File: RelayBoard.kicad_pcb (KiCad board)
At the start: 4 copper layers, 210.4 x 94.7 mm, 103 parts, among them J1 CONN_03-SCREW-5MM, J10 24VAC Input, J11 CONN_03-SCREW-5MM, J12 CONN_03-SCREW-5MM, J13 CONN_03-SCREW-5MM, J14 CONN_03-SCREW-5MM, J15 CONN_03-SCREW-5MM, J16 CONN_03-SCREW-5MM, J17 CONN_03-SCREW-5MM, J18 CONN_03-SCREW-5MM, J19 Raspberry_Pi_2_3, J2 CONN_03-SCREW-5MM, J22 Conn_01x04, J24 Conn_01x06, J3 CONN_03-SCREW-5MM, J4 CONN_03-SCREW-5MM, J5 CONN_03-SCREW-5MM, J6 CONN_03-SCREW-5MM, J7 CONN_03-SCREW-5MM, J8 CONN_03-SCREW-5MM, J9 DC Input, Q1 ULN2803ADWR, Q2 ULN2803ADWR, U1 TLP148G, U11 TLP148G, U12 TLP148G, U13 TLP148G, U14 TLP148G, U15 TLP148G, U16 TLP148G, U17 TLP148G, U18 TLP148G, U2 TLP148G, U3 TLP148G, U4 TLP148G, U5 TLP148G, U6 TLP148G, U7 TLP148G, U8 TLP148G

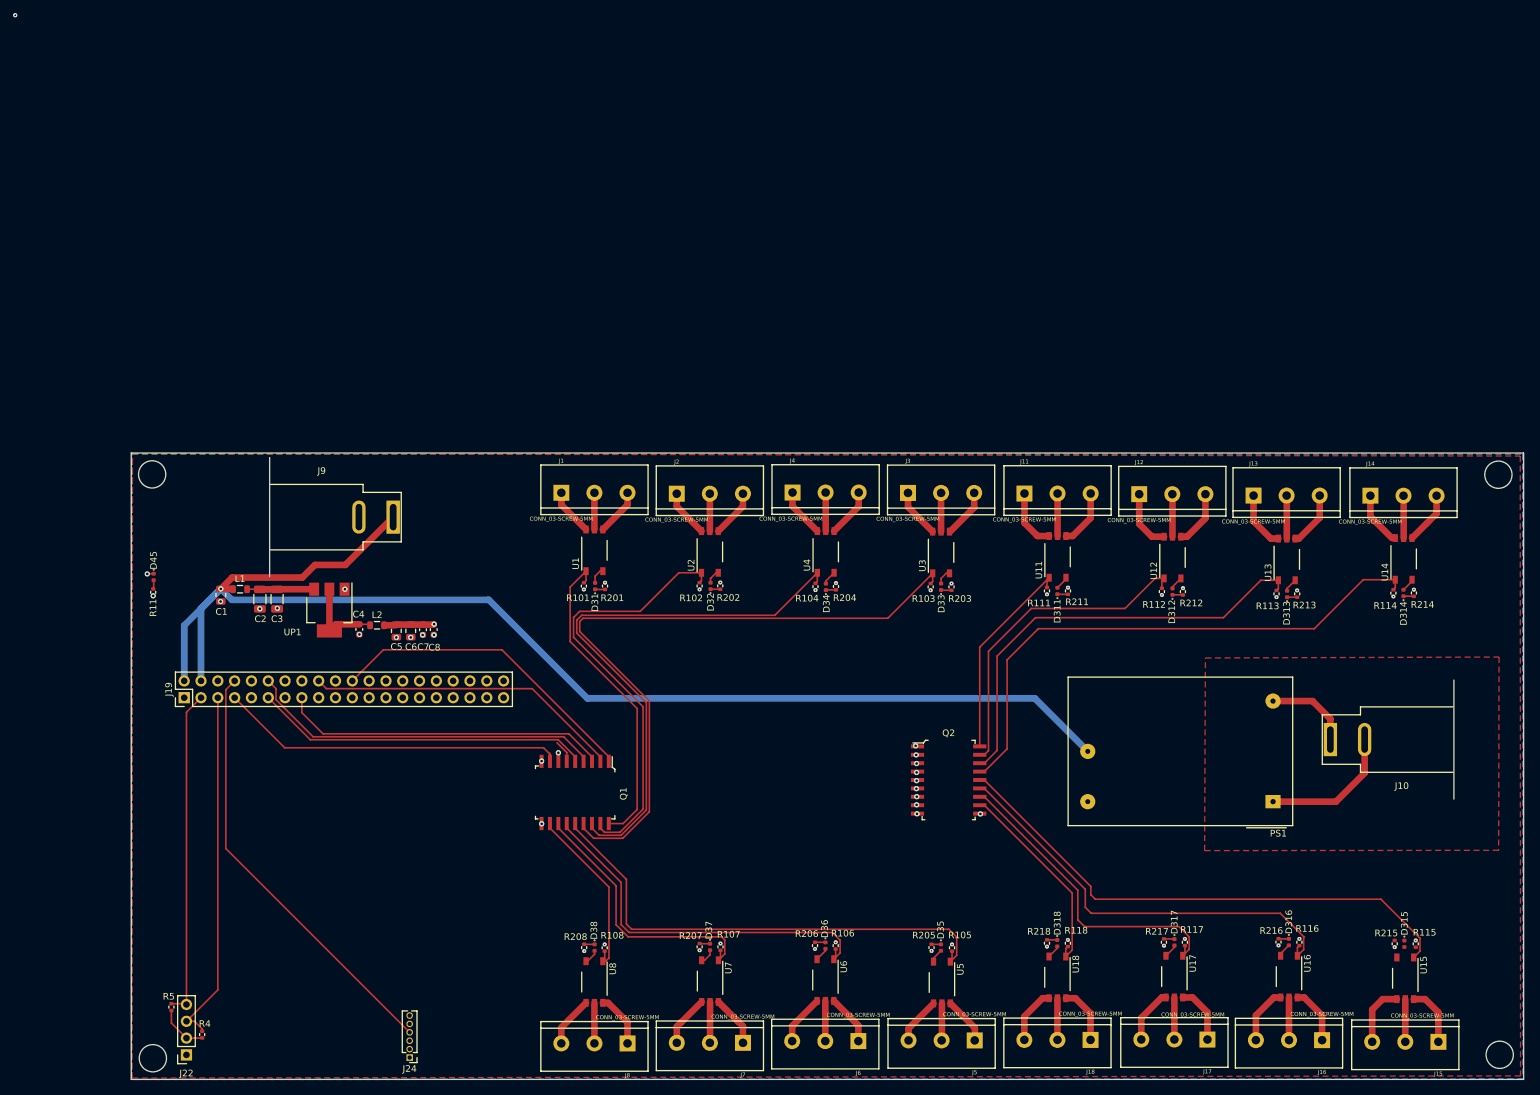
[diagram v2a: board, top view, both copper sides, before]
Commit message: replace connectors, reroute GPIOs and power
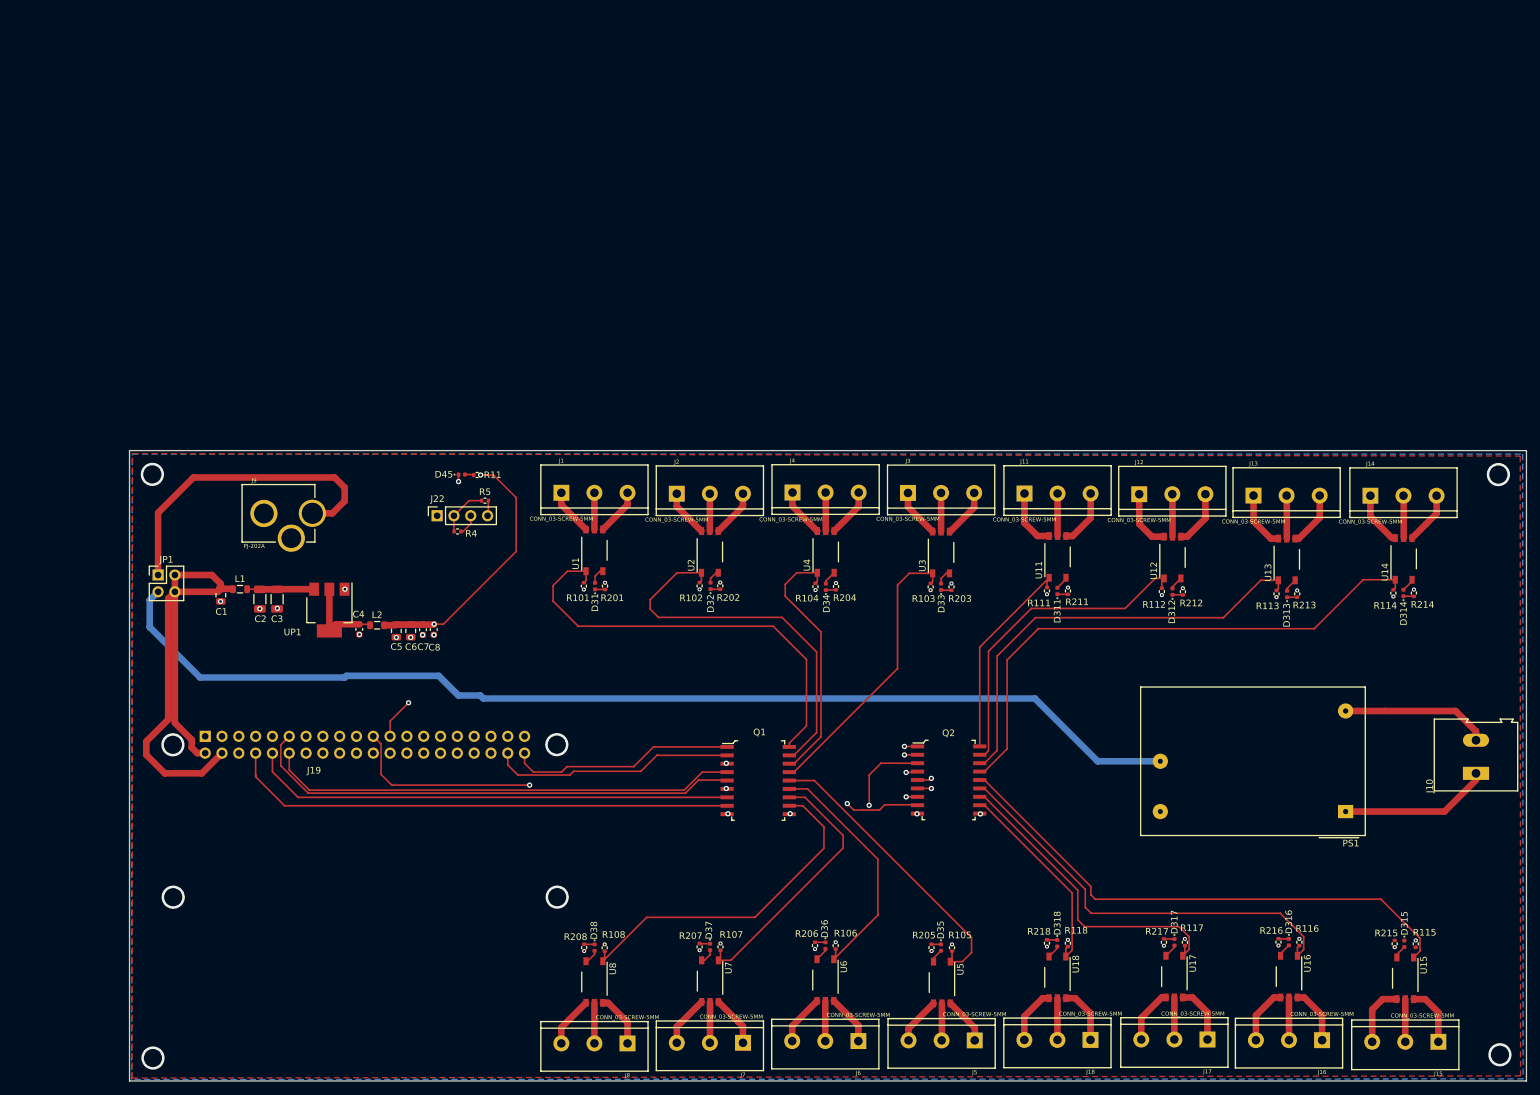
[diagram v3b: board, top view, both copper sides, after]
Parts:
- removed J24: Conn_01x06, Connector_PinHeader_1.27mm:PinHeader_1x06_P1.27mm_Vertical
- added JP1: VBUS Select, Connector_PinHeader_2.54mm:PinHeader_2x02_P2.54mm_Vertical, F.Cu at (21.6, 84.6)
- J10: value 24VAC Input -> AC In; footprint Connector_BarrelJack:BarrelJack_SwitchcraftConxall_RAPC10U_Horizontal -> TerminalBlock:TerminalBlock_Altech_AK300-2_P5.00mm
- J19: moved to B.Cu
- J9: value DC Input -> PJ-202A; footprint Connector_BarrelJack:BarrelJack_SwitchcraftConxall_RAPC10U_Horizontal -> Connectors:POWER_JACK_PTH_LOCK
- moved R5 90.0 mm to (71.0, 73.4), turned to 0 degrees
- moved J22 89.8 mm to (63.8, 75.6), turned to 90 degrees
- moved R4 85.3 mm to (66.8, 78.0), turned to 0 degrees
- moved R11 52.1 mm to (69.8, 69.5), turned to 180 degrees
- moved D45 49.1 mm to (67.5, 69.4), turned to 0 degrees
- moved Q1 27.7 mm to (112.3, 115.6), turned to -90 degrees
- moved J9 26.1 mm to (31.0, 75.3), turned to -90 degrees
- moved J10 22.6 mm to (220.7, 114.6), turned to 90 degrees
- moved PS1 11.1 mm to (201.0, 120.3)
- moved J19 6.64 mm to (28.7, 109.0), turned to -90 degrees
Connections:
- J10 pad 1: Net-(J10-Pad1) -> AC_N_In
- J10 pad 2: Net-(J10-Pad2) -> AC_L_In
- J19 pad 10: USART_RX -> Net-(J19-Pad10)
- J19 pad 15: Net-(Q1-Pad3) -> unconnected-(J19-Pad15)
- J19 pad 18: Net-(Q1-Pad2) -> unconnected-(J19-Pad18)
- J19 pad 22: Net-(Q1-Pad1) -> unconnected-(J19-Pad22)
- J19 pad 27: Net-(Q1-Pad7) -> unconnected-(J19-Pad27)
- J19 pad 35: unconnected-(J19-Pad35) -> Net-(J19-Pad35)
- J19 pad 38: unconnected-(J19-Pad38) -> Net-(J19-Pad38)
- J19 pad 40: unconnected-(J19-Pad40) -> Net-(Q1-Pad1)
- J19 pad 7: Net-(Q1-Pad8) -> unconnected-(J19-Pad7)
- J19 pad 8: USART_TX -> Net-(J19-Pad8)
- PS1 pad 1: Net-(J10-Pad2) -> AC_N_In
- PS1 pad 2: Net-(J10-Pad1) -> AC_L_In
- PS1 pad 4: VBUS -> Net-(PS1-Pad4)
- Q1 pad 2: Net-(Q1-Pad2) -> Net-(J19-Pad38)
- Q1 pad 3: Net-(Q1-Pad3) -> Net-(J19-Pad35)
- Q1 pad 7: Net-(Q1-Pad7) -> Net-(J19-Pad10)
- Q1 pad 8: Net-(Q1-Pad8) -> Net-(J19-Pad8)
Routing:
- net Net-(PS1-Pad4): track 0.00 -> 167.2 mm
- net VBUS: track 204.9 -> 87.0 mm, vias 1 -> 0
- net Net-(Q2-Pad5): track 5.04 -> 99.7 mm
- net Net-(Q2-Pad6): track 4.80 -> 98.9 mm, vias 1 -> 2
- net Net-(Q2-Pad4): track 5.36 -> 93.0 mm, vias 1 -> 2
- net Net-(Q2-Pad3): track 5.41 -> 90.4 mm
- net Net-(J19-Pad8): track 0.00 -> 76.6 mm
- net USART_RX: track 73.4 -> 0.00 mm
- net Net-(J19-Pad10): track 0.00 -> 73.1 mm
- net Net-(Q2-Pad7): track 5.04 -> 78.1 mm
- net Net-(Q2-Pad8): track 4.92 -> 76.1 mm
- net Net-(Q2-Pad1): track 5.47 -> 75.3 mm
- net Net-(Q2-Pad2): track 5.62 -> 73.0 mm
- net USART_TX: track 65.2 -> 0.00 mm
- net Net-(Q1-Pad15): track 104.0 -> 43.2 mm
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- removed copper zone on F.Cu, net (none)
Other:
- board size 210.4 x 94.7 mm -> 211.1 x 95.2 mm

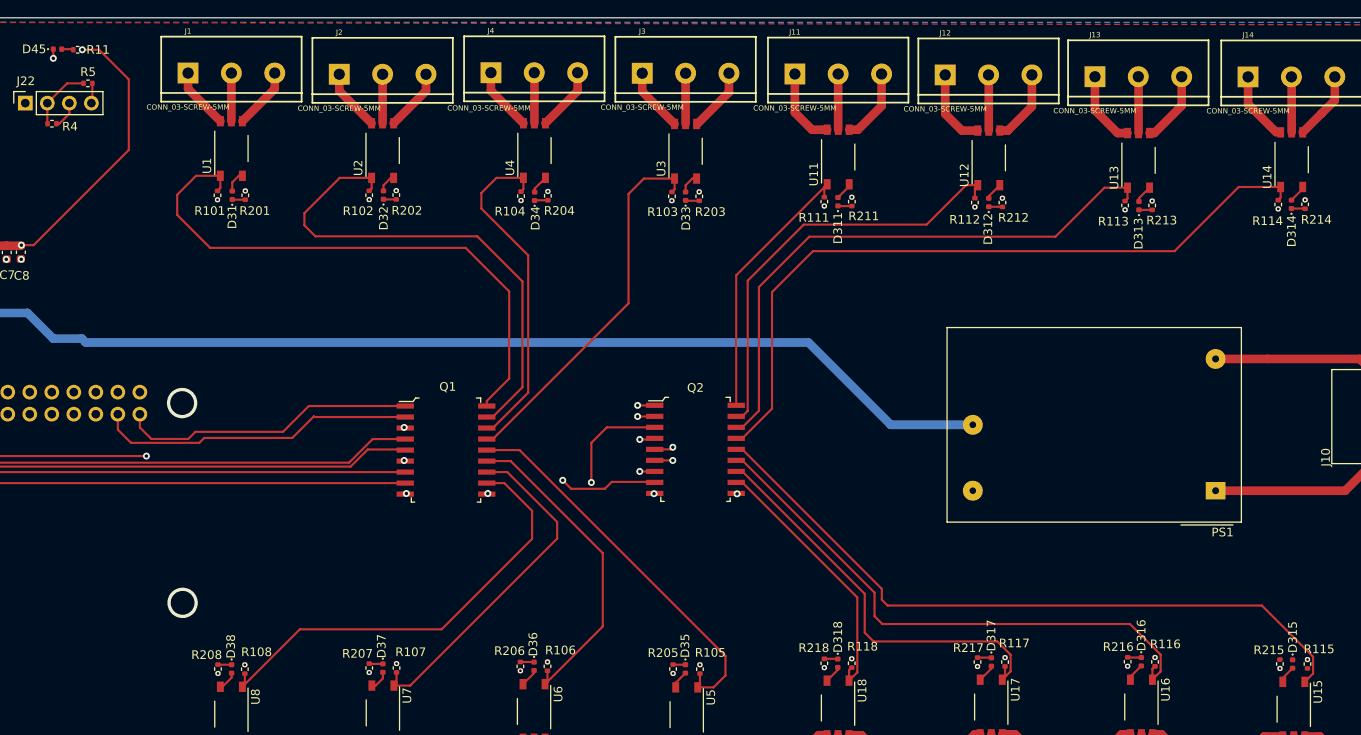
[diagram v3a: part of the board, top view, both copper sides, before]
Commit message: fix DRC errors, passes all tests
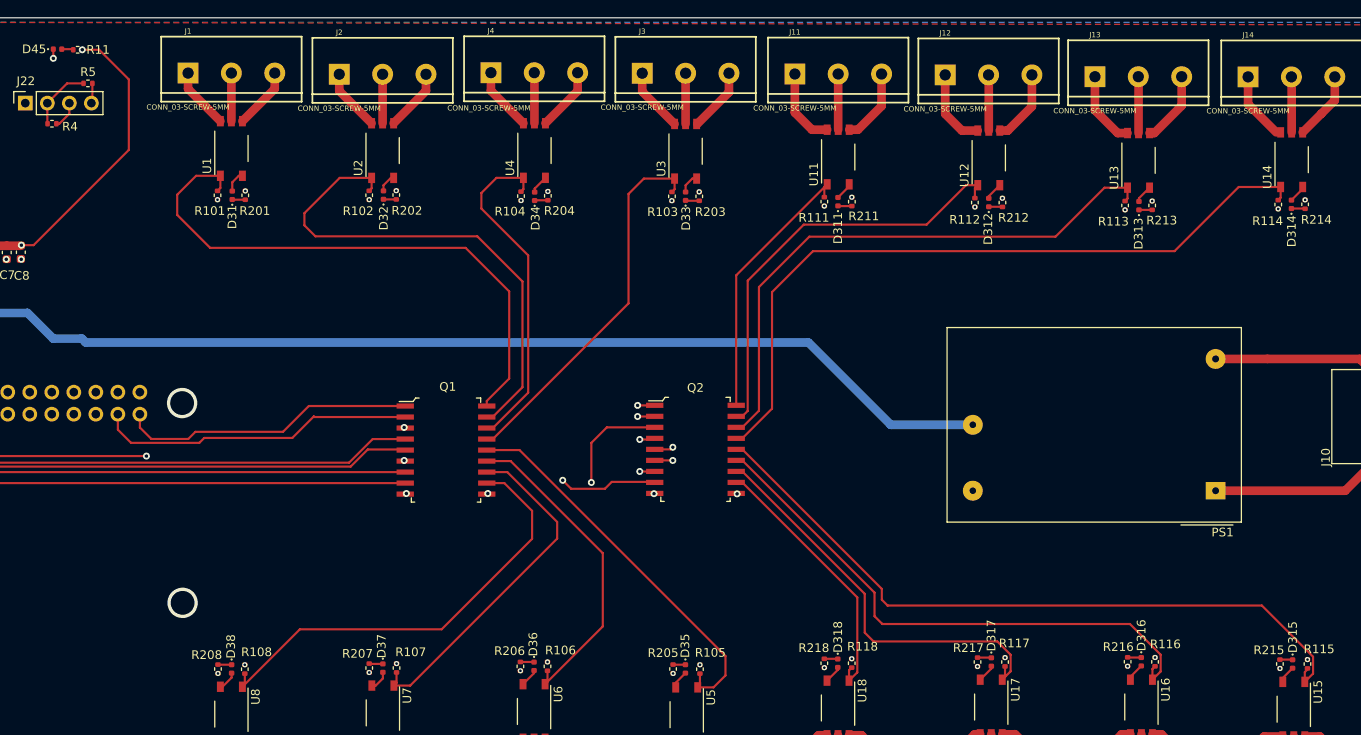
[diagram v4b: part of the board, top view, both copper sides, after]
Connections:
- J9 pad PWR: (no net) -> DC_IN
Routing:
- net Net-(Q2-Pad14): track 80.5 -> 82.1 mm
- net Net-(D315-Pad1): track 0.00 -> 1.47 mm
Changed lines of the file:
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@@
       (solder_mask_margin 0.1016))
     (pad "PWR" thru_hole circle locked (at 0 -13.87602 270) (size 4.1148 4.1148) (drill 3.19786) (layers *.Cu *.Mask)
-      (solder_mask_margin 0.1016))
+      (net 134 "DC_IN") (solder_mask_margin 0.1016))
   )
   (footprint "Resistor_SMD:R_0402_1005Metric" (layer "F.Cu")
@@
     )
   )
-  (gr_line (start 17.272 65.786) (end 17.272 161.036) (layer "Edge.Cuts") (width 0.1))
   (gr_line (start 228.346 65.786) (end 17.272 65.786) (layer "Edge.Cuts") (width 0.1))
+  (gr_line (start 17.272 65.786) (end 17.272 161.036) (layer "Edge.Cuts") (width 0.1))
   (gr_line (start 17.272 161.036) (end 228.346 161.036) (layer "Edge.Cuts") (width 0.1))
   (gr_line (start 228.346 161.036) (end 228.346 65.786) (layer "Edge.Cuts") (width 0.1))
@@
   (segment (start 24.13 87.122) (end 24.13 106.934) (width 1) (layer "F.Cu") (net 1))
   (segment (start 138.32587 86.89) (end 138.32629 86.88958) (width 0.25) (layer "F.Cu") (net 2))
-  (segment (start 66.96 69.38) (end 66.985 69.405) (width 0.25) (layer "F.Cu") (net 2))
-  (segment (start 85.82246 86.868) (end 85.9213 86.76916) (width 0.25) (layer "F.Cu") (net 2))
   (segment (start 155.90001 87.495) (end 156.075 87.495) (width 0.25) (layer "F.Cu") (net 2))
   (segment (start 66.985 69.405) (end 66.985 70.465774) (width 0.25) (layer "F.Cu") (net 2))
   (segment (start 208.23958 87.83) (end 208.245 87.83542) (width 0.25) (layer "F.Cu") (net 2))
-  (segment (start 103.41087 86.76) (end 103.41129 86.75958) (width 0.25) (layer "F.Cu") (net 2))
   (segment (start 66.985 70.465774) (end 66.985857 70.466631) (width 0.25) (layer "F.Cu") (net 2))
-  (segment (start 190.57374 87.93) (end 190.585 87.94126) (width 0.25) (layer "F.Cu") (net 2))
-  (segment (start 173.24042 87.63) (end 173.265 87.60542) (width 0.25) (layer "F.Cu") (net 2))
   (via (at 123.976119 140.073969) (size 0.6) (drill 0.3) (layers "F.Cu" "B.Cu") (free) (net 2))
   (via (at 107.696 120.65) (size 0.8) (drill 0.4) (layers "F.Cu" "B.Cu") (net 2))
@@
   (via (at 120.849201 141.098295) (size 0.6) (drill 0.3) (layers "F.Cu" "B.Cu") (free) (net 2))
   (via (at 106.568822 140.264737) (size 0.6) (drill 0.3) (layers "F.Cu" "B.Cu") (free) (net 2))
-  (via (at 85.918234 86.77662) (size 0.6) (drill 0.3) (layers "F.Cu" "B.Cu") (free) (net 2))
+  (via (at 85.921221 86.772762) (size 0.6) (drill 0.3) (layers "F.Cu" "B.Cu") (free) (net 2))
   (via (at 173.570322 140.601886) (size 0.6) (drill 0.3) (layers "F.Cu" "B.Cu") (free) (net 2))
   (via (at 159.060464 139.711488) (size 0.6) (drill 0.3) (layers "F.Cu" "B.Cu") (free) (net 2))
@@
   (via (at 103.417572 141.290268) (size 0.6) (drill 0.3) (layers "F.Cu" "B.Cu") (free) (net 2))
   (via (at 176.434601 86.591867) (size 0.6) (drill 0.3) (layers "F.Cu" "B.Cu") (free) (net 2))
-  (via (at 103.417901 86.75827) (size 0.6) (drill 0.3) (layers "F.Cu" "B.Cu") (free) (net 2))
-  (via (at 190.583272 87.9337) (size 0.6) (drill 0.3) (layers "F.Cu" "B.Cu") (free) (net 2))
+  (via (at 103.412842 86.763314) (size 0.6) (drill 0.3) (layers "F.Cu" "B.Cu") (free) (net 2))
+  (via (at 190.582894 87.940916) (size 0.6) (drill 0.3) (layers "F.Cu" "B.Cu") (free) (net 2))
   (via (at 141.471017 85.862822) (size 0.6) (drill 0.3) (layers "F.Cu" "B.Cu") (free) (net 2))
   (via (at 57.59 94.02) (size 0.8) (drill 0.4) (layers "F.Cu" "B.Cu") (net 2))
@@
   (via (at 23.872154 133.267037) (size 3.5) (drill 2.75) (layers "F.Cu" "B.Cu") (free) (net 2))
   (via (at 85.973336 141.40193) (size 0.6) (drill 0.3) (layers "F.Cu" "B.Cu") (free) (net 2))
-  (via (at 173.265065 87.611467) (size 0.6) (drill 0.3) (layers "F.Cu" "B.Cu") (free) (net 2))
+  (via (at 173.266524 87.610615) (size 0.6) (drill 0.3) (layers "F.Cu" "B.Cu") (free) (net 2))
   (via (at 36.96 89.69) (size 0.8) (drill 0.4) (layers "F.Cu" "B.Cu") (net 2))
   (via (at 176.742452 139.579314) (size 0.6) (drill 0.3) (layers "F.Cu" "B.Cu") (free) (net 2))
@@
   (segment (start 211.065 85.30042) (end 211.065 85.52042) (width 0.25) (layer "F.Cu") (net 91))
   (segment (start 211.065 85.52042) (end 209.77 86.81542) (width 0.25) (layer "F.Cu") (net 91))
+  (segment (start 208.44 139.80128) (end 209.875 139.80128) (width 0.25) (layer "F.Cu") (net 92))
+  (segment (start 209.875 139.80128) (end 209.9 139.82628) (width 0.25) (layer "F.Cu") (net 92))
   (segment (start 190.905 139.56628) (end 190.88 139.54128) (width 0.25) (layer "F.Cu") (net 93))
   (segment (start 192.45 139.56628) (end 190.905 139.56628) (width 0.25) (layer "F.Cu") (net 93))
@@
   (segment (start 145.74 115.56) (end 146.44 115.56) (width 0.25) (layer "F.Cu") (net 106))
   (segment (start 162.53 132.9) (end 163.19 133.56) (width 0.25) (layer "F.Cu") (net 106))
+  (segment (start 211.31 141.242) (end 211.31 142.37128) (width 0.25) (layer "F.Cu") (net 106))
   (segment (start 163.19 133.56) (end 163.19 133.57) (width 0.25) (layer "F.Cu") (net 106))
+  (segment (start 211.62 140.932) (end 211.31 141.242) (width 0.25) (layer "F.Cu") (net 106))
   (segment (start 146.44 115.56) (end 162.53 131.65) (width 0.25) (layer "F.Cu") (net 106))
   (segment (start 212.26452 141.41676) (end 211.31 142.37128) (width 0.25) (layer "F.Cu") (net 106))
   (segment (start 212.26452 139.475941) (end 212.26452 141.41676) (width 0.25) (layer "F.Cu") (net 106))
   (segment (start 206.358579 133.57) (end 212.26452 139.475941) (width 0.25) (layer "F.Cu") (net 106))
+  (segment (start 211.62 140.82128) (end 211.62 140.932) (width 0.25) (layer "F.Cu") (net 106))
   (segment (start 162.53 131.65) (end 162.53 132.9) (width 0.25) (layer "F.Cu") (net 106))
   (segment (start 163.19 133.57) (end 206.358579 133.57) (width 0.25) (layer "F.Cu") (net 106))
